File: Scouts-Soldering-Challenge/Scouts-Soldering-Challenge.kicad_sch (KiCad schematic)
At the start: 13 parts, among them SW1 SW_Push

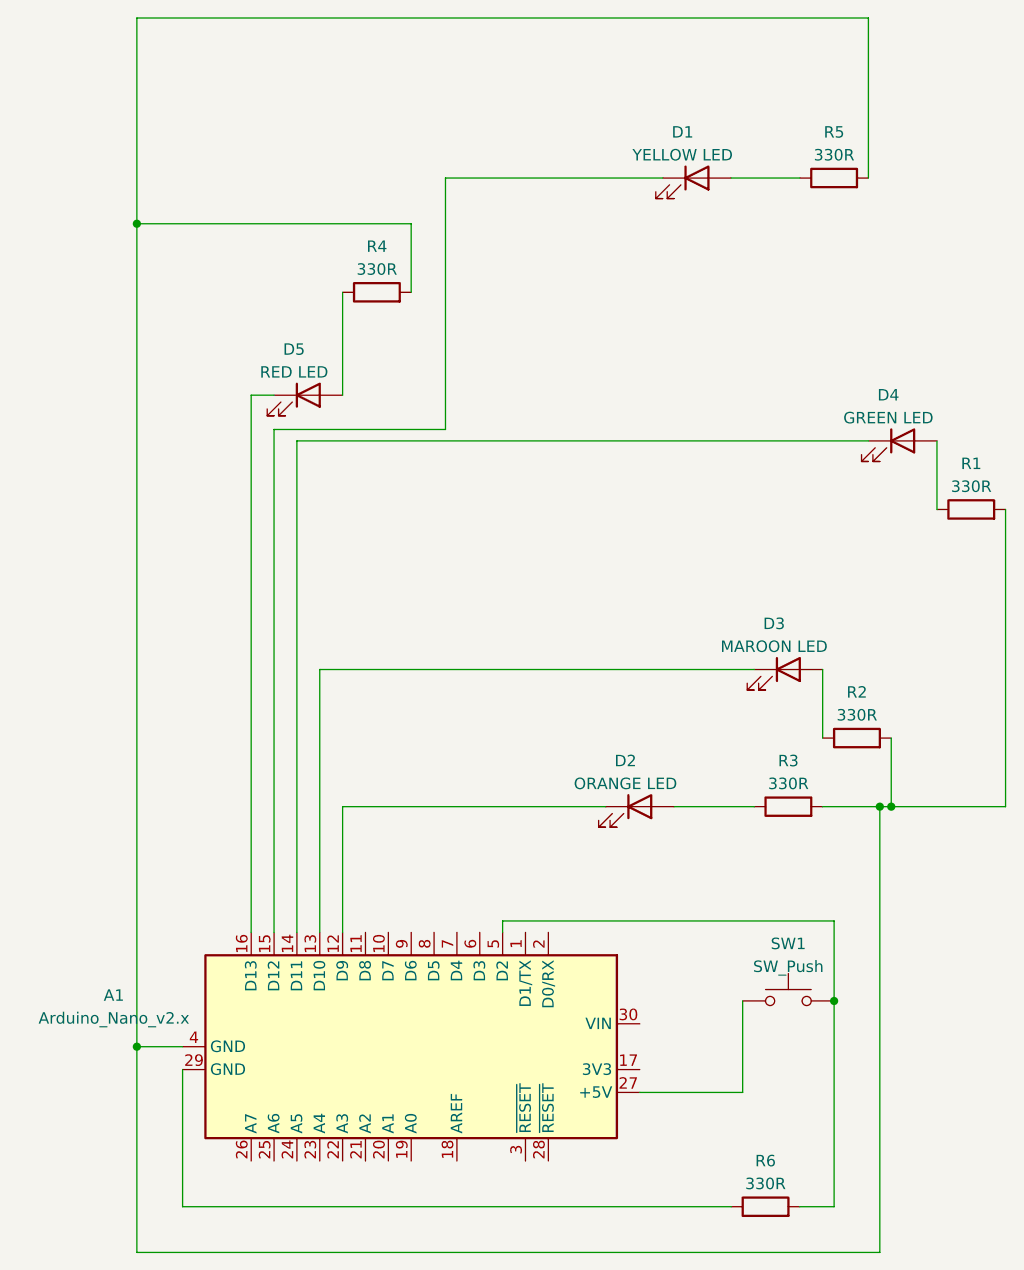
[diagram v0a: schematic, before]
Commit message: Corrected mistake in PCB
Wiring is all still the same, but the pins on the LED were connected in the wrong orientation, meaning the PCB showed the LED rotated the wrong way.
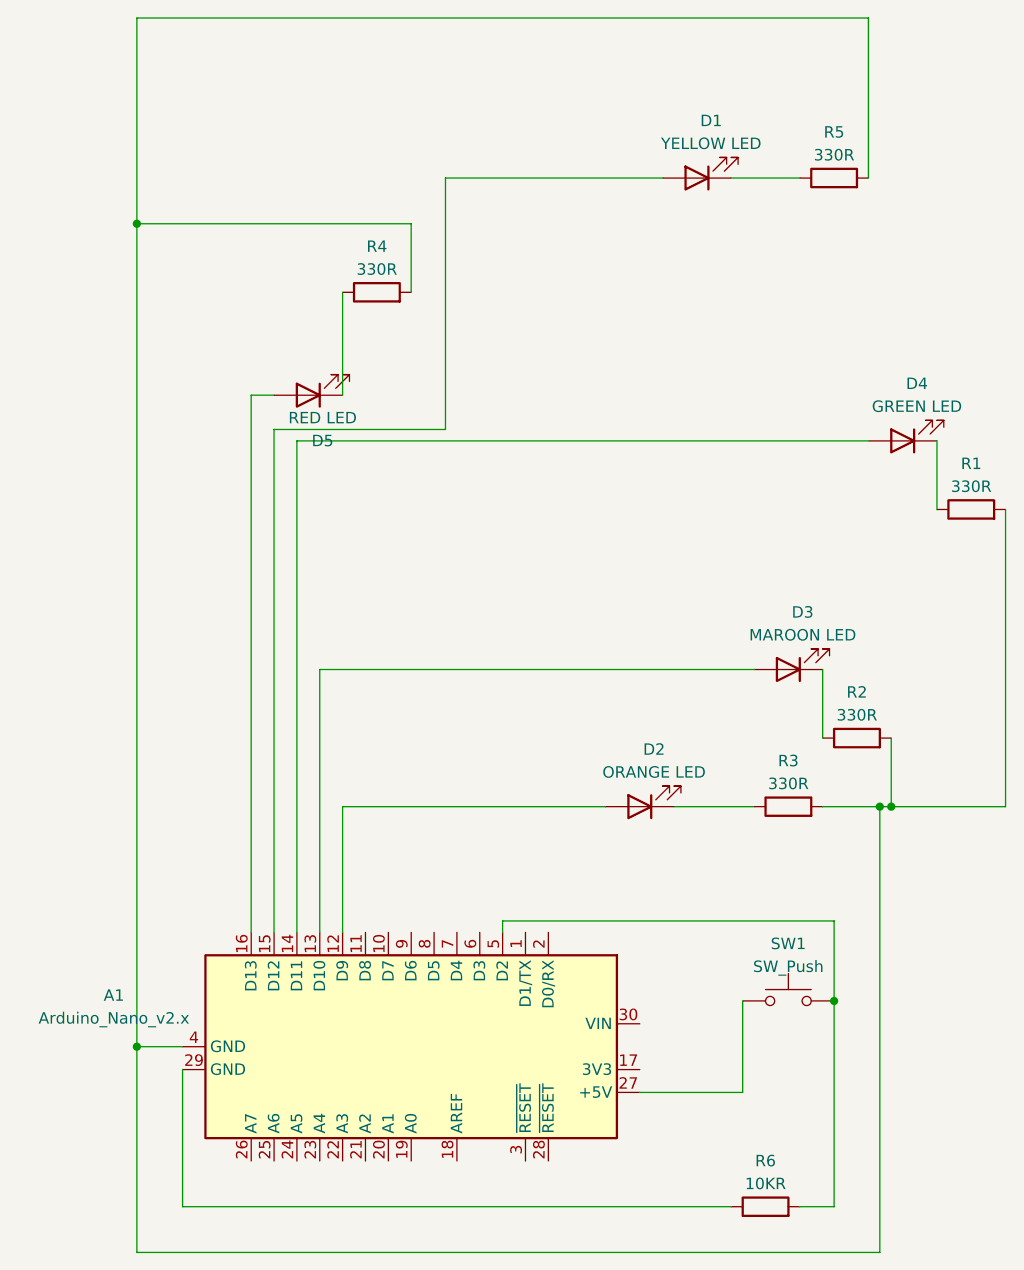
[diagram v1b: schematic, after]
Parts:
- R6: value 330R -> 10KR
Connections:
- net at R5.1: now also D1.1 (K); no longer D1.2 (A)
- net at R3.1: now also D2.1 (K); no longer D2.2 (A)
- net at D4.1 (K): now also R1.1; no longer A1.14 (D11)
- net at D4.2 (A): now also A1.14 (D11); no longer R1.1
- net at D5.1 (K): now also R4.1; no longer A1.16 (D13)
- net at D5.2 (A): now also A1.16 (D13); no longer R4.1
- net at A1.12 (D9): now also D2.2 (A); no longer D2.1 (K)
- net at A1.13 (D10): now also D3.2 (A); no longer D3.1 (K)
- net at A1.15 (D12): now also D1.2 (A); no longer D1.1 (K)
- net at R2.1: now also D3.1 (K); no longer D3.2 (A)
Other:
- moved on the sheet: D1, D2, D3, D4, D5
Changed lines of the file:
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@@
-    (stroke (width 0) (type default))
-  )
-  (wire (pts (xy 87.63 80.01) (xy 68.58 80.01))
     (stroke (width 0) (type default))
   )
@@
   )
   (wire (pts (xy 134.62 52.07) (xy 134.62 34.29))
+    (stroke (width 0) (type default))
+  )
+  (wire (pts (xy 68.58 80.01) (xy 87.63 80.01))
     (stroke (width 0) (type default))
   )
@@
     )
   )
-  (symbol (lib_id "Device:LED") (at 138.43 81.28 0) (unit 1)
+  (symbol (lib_id "Device:LED") (at 138.43 81.28 180) (unit 1)
     (in_bom yes) (on_board yes) (dnp no) (fields_autoplaced)
-    (property "Reference" "D4" (at 136.8425 76.2 0)
-      (effects (font (size 1.27 1.27)))
-    )
-    (property "Value" "GREEN LED" (at 136.8425 78.74 0)
+    (property "Reference" "D4" (at 140.0175 74.93 0)
+      (effects (font (size 1.27 1.27)))
+    )
+    (property "Value" "GREEN LED" (at 140.0175 77.47 0)
       (effects (font (size 1.27 1.27)))
     )
@@
       (effects (font (size 1.27 1.27)))
     )
-    (property "Value" "330R" (at 123.19 163.83 90)
+    (property "Value" "10KR" (at 123.19 163.83 90)
       (effects (font (size 1.27 1.27)))
     )
@@
     )
   )
-  (symbol (lib_id "Device:LED") (at 72.39 76.2 0) (unit 1)
+  (symbol (lib_id "Device:LED") (at 72.39 76.2 180) (unit 1)
     (in_bom yes) (on_board yes) (dnp no)
-    (property "Reference" "D5" (at 70.8025 71.12 0)
-      (effects (font (size 1.27 1.27)))
-    )
-    (property "Value" "RED LED" (at 70.8025 73.66 0)
+    (property "Reference" "D5" (at 73.9775 81.28 0)
+      (effects (font (size 1.27 1.27)))
+    )
+    (property "Value" "RED LED" (at 73.9775 78.74 0)
       (effects (font (size 1.27 1.27)))
     )
@@
     )
   )
-  (symbol (lib_id "Device:LED") (at 109.22 121.92 0) (unit 1)
+  (symbol (lib_id "Device:LED") (at 109.22 121.92 180) (unit 1)
     (in_bom yes) (on_board yes) (dnp no) (fields_autoplaced)
-    (property "Reference" "D2" (at 107.6325 116.84 0)
-      (effects (font (size 1.27 1.27)))
-    )
-    (property "Value" "ORANGE LED" (at 107.6325 119.38 0)
+    (property "Reference" "D2" (at 110.8075 115.57 0)
+      (effects (font (size 1.27 1.27)))
+    )
+    (property "Value" "ORANGE LED" (at 110.8075 118.11 0)
       (effects (font (size 1.27 1.27)))
     )
@@
     )
   )
-  (symbol (lib_id "Device:LED") (at 115.57 52.07 0) (unit 1)
+  (symbol (lib_id "Device:LED") (at 115.57 52.07 180) (unit 1)
     (in_bom yes) (on_board yes) (dnp no) (fields_autoplaced)
-    (property "Reference" "D1" (at 113.9825 46.99 0)
-      (effects (font (size 1.27 1.27)))
-    )
-    (property "Value" "YELLOW LED" (at 113.9825 49.53 0)
+    (property "Reference" "D1" (at 117.1575 45.72 0)
+      (effects (font (size 1.27 1.27)))
+    )
+    (property "Value" "YELLOW LED" (at 117.1575 48.26 0)
       (effects (font (size 1.27 1.27)))
     )
@@
     )
   )
-  (symbol (lib_id "Device:LED") (at 125.73 106.68 0) (unit 1)
+  (symbol (lib_id "Device:LED") (at 125.73 106.68 180) (unit 1)
     (in_bom yes) (on_board yes) (dnp no) (fields_autoplaced)
-    (property "Reference" "D3" (at 124.1425 101.6 0)
-      (effects (font (size 1.27 1.27)))
-    )
-    (property "Value" "MAROON LED" (at 124.1425 104.14 0)
-      (effects (font (size 1.27 1.27)))
-    )
+    (property "Reference" "D3" (at 127.3175 100.33 0)
+      (effects (font (size 1.27 1.27)))
+    )
+    (property "Value" "MAROON LED" (at 127.3175 102.87 0)
+      (effects (font (size 1.27 1.27)))
+    )
